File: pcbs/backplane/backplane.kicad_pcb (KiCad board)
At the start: 2 copper layers, 80 x 50 mm, 59 parts, among them P1 USB_B, P3 CONN_02X03, P4 CONN_02X03, P5 CONN_02X07, P6 CONN_02X07, P7 CONN_01X03, P8 CONN_01X03, Q1 MMBT3904, Q2 MMBT3904, Q3 Si2323, U1 LM358, U2 TC1262-33VDB, U3 LM358, U4 CH340G, Y1 Crystal

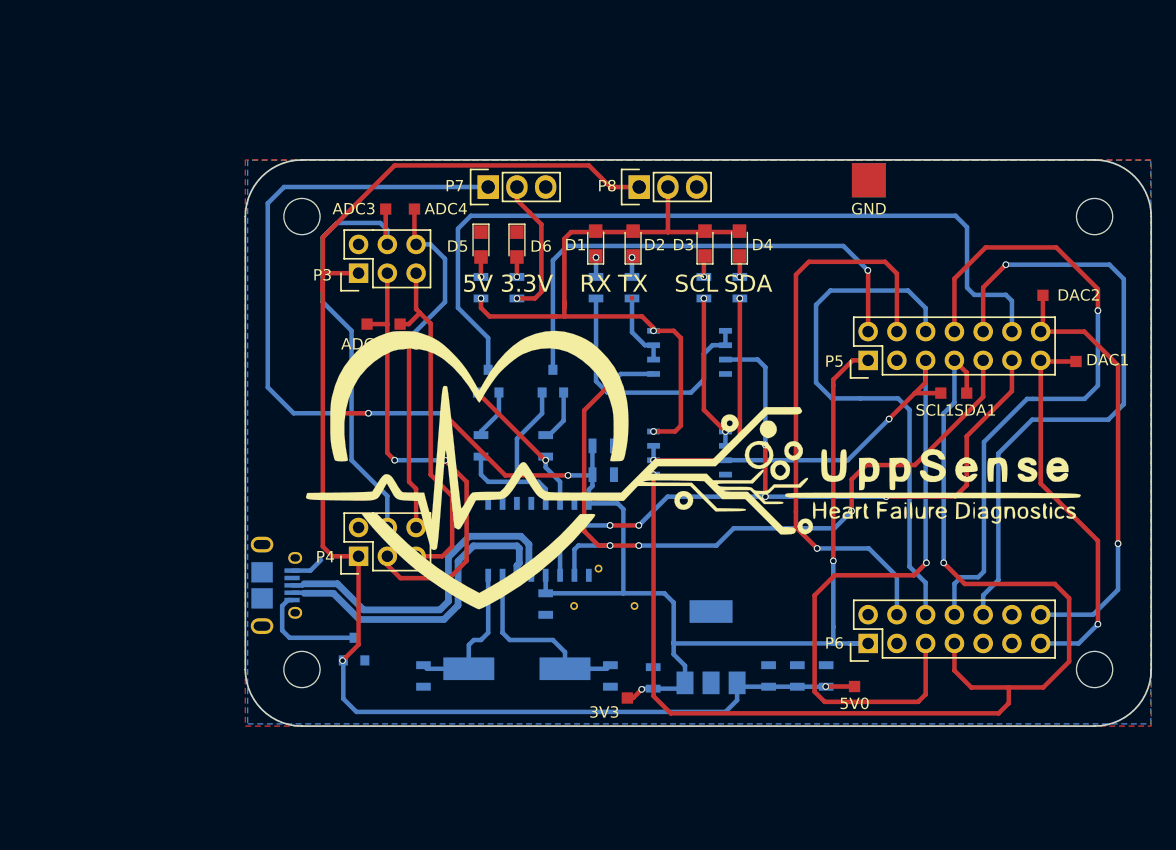
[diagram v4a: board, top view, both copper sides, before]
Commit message: Simulated the new transimpedance amp.
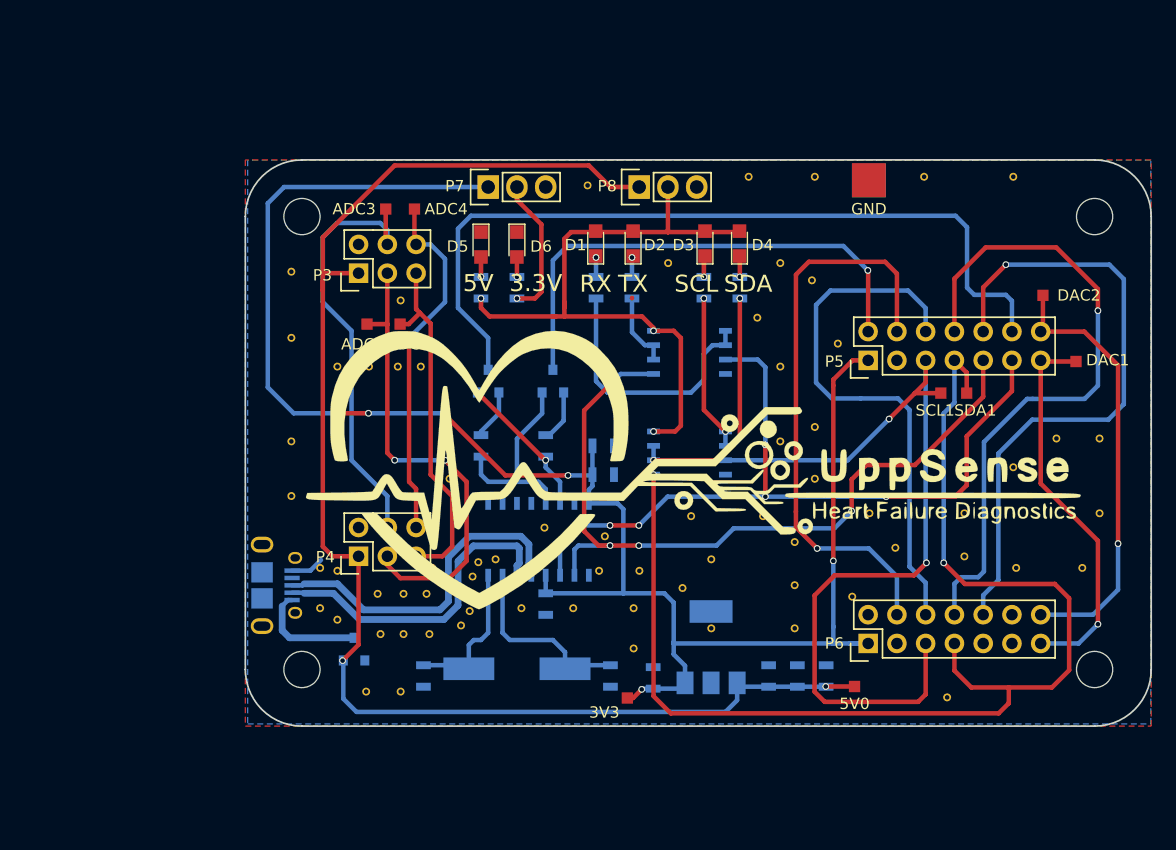
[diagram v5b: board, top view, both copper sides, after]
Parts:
- added REF**: Stitching-Via-0.5-0.7, myVias:Stitchging-Via-0.4-0.7, F.Cu at (182.3, 67.7)
- added REF**: Stitching-Via-0.5-0.7, myVias:Stitchging-Via-0.4-0.7, F.Cu at (122.6, 106.8)
- added REF**: Stitching-Via-0.5-0.7, myVias:Stitchging-Via-0.4-0.7, F.Cu at (121.1, 105.8)
- added REF**: Stitching-Via-0.5-0.7, myVias:Stitchging-Via-0.4-0.7, F.Cu at (122.6, 102.5)
- added REF**: Stitching-Via-0.5-0.7, myVias:Stitchging-Via-0.4-0.7, F.Cu at (134.3, 106.1)
- added REF**: Stitching-Via-0.5-0.7, myVias:Stitchging-Via-0.4-0.7, F.Cu at (134.5, 104.5)
- added REF**: Stitching-Via-0.5-0.7, myVias:Stitchging-Via-0.4-0.7, F.Cu at (130.7, 108.1)
- added REF**: Stitching-Via-0.5-0.7, myVias:Stitchging-Via-0.4-0.7, F.Cu at (126.4, 108.1)
- added REF**: Stitching-Via-0.5-0.7, myVias:Stitchging-Via-0.4-0.7, F.Cu at (130.5, 104.5)
- added REF**: Stitching-Via-0.5-0.7, myVias:Stitchging-Via-0.4-0.7, F.Cu at (126.2, 104.5)
- added REF**: Stitching-Via-0.5-0.7, myVias:Stitchging-Via-0.4-0.7, F.Cu at (164.8, 94.4)
- added REF**: Stitching-Via-0.5-0.7, myVias:Stitchging-Via-0.4-0.7, F.Cu at (174.4, 67.7)
- added REF**: Stitching-Via-0.5-0.7, myVias:Stitchging-Via-0.4-0.7, F.Cu at (164.8, 89.8)
- added REF**: Stitching-Via-0.5-0.7, myVias:Stitchging-Via-0.4-0.7, F.Cu at (166.8, 82.4)
- added REF**: Stitching-Via-0.5-0.7, myVias:Stitchging-Via-0.4-0.7, F.Cu at (164.5, 76.9)
- added REF**: Stitching-Via-0.5-0.7, myVias:Stitchging-Via-0.4-0.7, F.Cu at (144.7, 68.5)
- added REF**: Stitching-Via-0.5-0.7, myVias:Stitchging-Via-0.4-0.7, F.Cu at (128.2, 78.6)
- added REF**: Stitching-Via-0.5-0.7, myVias:Stitchging-Via-0.4-0.7, F.Cu at (132.5, 94.4)
- added REF**: Stitching-Via-0.5-0.7, myVias:Stitchging-Via-0.4-0.7, F.Cu at (130.0, 84.5)
- added REF**: Stitching-Via-0.5-0.7, myVias:Stitchging-Via-0.4-0.7, F.Cu at (127.9, 84.5)
- added REF**: Stitching-Via-0.5-0.7, myVias:Stitchging-Via-0.4-0.7, F.Cu at (125.4, 84.5)
- added REF**: Stitching-Via-0.5-0.7, myVias:Stitchging-Via-0.4-0.7, F.Cu at (122.6, 84.5)
- added REF**: Stitching-Via-0.5-0.7, myVias:Stitchging-Via-0.4-0.7, F.Cu at (164.8, 67.7)
- added REF**: Stitching-Via-0.5-0.7, myVias:Stitchging-Via-0.4-0.7, F.Cu at (118.5, 95.9)
- added REF**: Stitching-Via-0.5-0.7, myVias:Stitchging-Via-0.4-0.7, F.Cu at (118.5, 81.9)
- added REF**: Stitching-Via-0.5-0.7, myVias:Stitchging-Via-0.4-0.7, F.Cu at (118.5, 76.1)
- added REF**: Stitching-Via-0.5-0.7, myVias:Stitchging-Via-0.4-0.7, F.Cu at (118.5, 91.1)
- added REF**: Stitching-Via-0.5-0.7, myVias:Stitchging-Via-0.4-0.7, F.Cu at (121.1, 102.3)
- added REF**: Stitching-Via-0.5-0.7, myVias:Stitchging-Via-0.4-0.7, F.Cu at (128.4, 104.5)
- added REF**: Stitching-Via-0.5-0.7, myVias:Stitchging-Via-0.4-0.7, F.Cu at (133.5, 107.3)
- added REF**: Stitching-Via-0.5-0.7, myVias:Stitchging-Via-0.4-0.7, F.Cu at (134.5, 103.0)
- added REF**: Stitching-Via-0.5-0.7, myVias:Stitchging-Via-0.4-0.7, F.Cu at (128.2, 113.2)
- added REF**: Stitching-Via-0.5-0.7, myVias:Stitchging-Via-0.4-0.7, F.Cu at (128.4, 108.1)
- added REF**: Stitching-Via-0.5-0.7, myVias:Stitchging-Via-0.4-0.7, F.Cu at (158.9, 67.7)
- added REF**: Stitching-Via-0.5-0.7, myVias:Stitchging-Via-0.4-0.7, F.Cu at (125.1, 113.2)
- added REF**: Stitching-Via-0.5-0.7, myVias:Stitchging-Via-0.4-0.7, F.Cu at (140.9, 98.7)
- added REF**: Stitching-Via-0.5-0.7, myVias:Stitchging-Via-0.4-0.7, F.Cu at (146.2, 99.5)
- added REF**: Stitching-Via-0.5-0.7, myVias:Stitchging-Via-0.4-0.7, F.Cu at (160.2, 97.7)
- added REF**: Stitching-Via-0.5-0.7, myVias:Stitchging-Via-0.4-0.7, F.Cu at (153.8, 97.7)
- added REF**: Stitching-Via-0.5-0.7, myVias:Stitchging-Via-0.4-0.7, F.Cu at (151.8, 75.3)
- added REF**: Stitching-Via-0.5-0.7, myVias:Stitchging-Via-0.4-0.7, F.Cu at (159.7, 80.2)
- added REF**: Stitching-Via-0.5-0.7, myVias:Stitchging-Via-0.4-0.7, F.Cu at (161.7, 75.3)
- added REF**: Stitching-Via-0.5-0.7, myVias:Stitchging-Via-0.4-0.7, F.Cu at (161.7, 84.5)
- added REF**: Stitching-Via-0.5-0.7, myVias:Stitchging-Via-0.4-0.7, F.Cu at (161.7, 91.1)
- added REF**: Stitching-Via-0.5-0.7, myVias:Stitchging-Via-0.4-0.7, F.Cu at (168.1, 104.8)
- added REF**: Stitching-Via-0.5-0.7, myVias:Stitchging-Via-0.4-0.7, F.Cu at (189.9, 97.4)
- added REF**: Stitching-Via-0.5-0.7, myVias:Stitchging-Via-0.4-0.7, F.Cu at (186.1, 90.8)
- added REF**: Stitching-Via-0.5-0.7, myVias:Stitchging-Via-0.4-0.7, F.Cu at (189.9, 90.8)
- added REF**: Stitching-Via-0.5-0.7, myVias:Stitchging-Via-0.4-0.7, F.Cu at (188.4, 102.3)
- added REF**: Stitching-Via-0.5-0.7, myVias:Stitchging-Via-0.4-0.7, F.Cu at (182.3, 93.4)
- added REF**: Stitching-Via-0.5-0.7, myVias:Stitchging-Via-0.4-0.7, F.Cu at (182.5, 102.3)
- added REF**: Stitching-Via-0.5-0.7, myVias:Stitchging-Via-0.4-0.7, F.Cu at (178.0, 97.4)
- added REF**: Stitching-Via-0.5-0.7, myVias:Stitchging-Via-0.4-0.7, F.Cu at (178.0, 101.2)
- added REF**: Stitching-Via-0.5-0.7, myVias:Stitchging-Via-0.4-0.7, F.Cu at (169.6, 97.4)
- added REF**: Stitching-Via-0.5-0.7, myVias:Stitchging-Via-0.4-0.7, F.Cu at (171.9, 100.5)
- added REF**: Stitching-Via-0.5-0.7, myVias:Stitchging-Via-0.4-0.7, F.Cu at (176.5, 113.7)
- added REF**: Stitching-Via-0.5-0.7, myVias:Stitchging-Via-0.4-0.7, F.Cu at (155.6, 107.6)
- added REF**: Stitching-Via-0.5-0.7, myVias:Stitchging-Via-0.4-0.7, F.Cu at (153.1, 104.0)
- added REF**: Stitching-Via-0.5-0.7, myVias:Stitchging-Via-0.4-0.7, F.Cu at (149.3, 102.5)
- added REF**: Stitching-Via-0.5-0.7, myVias:Stitchging-Via-0.4-0.7, F.Cu at (155.6, 101.5)
- added REF**: Stitching-Via-0.5-0.7, myVias:Stitchging-Via-0.4-0.7, F.Cu at (163.0, 100.0)
- added REF**: Stitching-Via-0.5-0.7, myVias:Stitchging-Via-0.4-0.7, F.Cu at (163.0, 103.8)
- added REF**: Stitching-Via-0.5-0.7, myVias:Stitchging-Via-0.4-0.7, F.Cu at (163.0, 107.6)
- added REF**: Stitching-Via-0.5-0.7, myVias:Stitchging-Via-0.4-0.7, F.Cu at (138.9, 105.8)
- added REF**: Stitching-Via-0.5-0.7, myVias:Stitchging-Via-0.4-0.7, F.Cu at (148.8, 109.4)
- added REF**: Stitching-Via-0.5-0.7, myVias:Stitchging-Via-0.4-0.7, F.Cu at (131.0, 102.3)
- added REF**: Stitching-Via-0.5-0.7, myVias:Stitchging-Via-0.4-0.7, F.Cu at (136.6, 101.5)
- added REF**: Stitching-Via-0.5-0.7, myVias:Stitchging-Via-0.4-0.7, F.Cu at (135.1, 101.7)
- moved REF** 0.21 mm to (148.8, 105.8)
- moved REF** 0.21 mm to (143.4, 105.8)
- moved REF** 0.20 mm to (145.7, 102.5)
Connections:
- P1 pad : (no net) -> GND

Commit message: Added some iportant backplane spec.
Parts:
- removed the REF** at (134.5, 104.5)
- removed the REF** at (135.1, 101.7)
- moved REF** 0.80 mm to (134.5, 105.3)
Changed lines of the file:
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@@
 (kicad_pcb (version 4) (host pcbnew 4.0.6-e0-6349~52~ubuntu17.04.1)
   (general
-    (links 179)
+    (links 177)
     (no_connects 0)
     (area 114.400999 66.146999 194.551001 116.297001)
@@
     (tracks 460)
     (zones 0)
-    (modules 127)
+    (modules 125)
     (nets 41)
   )
@@
   )
   (setup
-    (last_trace_width 0.4)
+    (last_trace_width 0.25)
     (user_trace_width 0.2)
     (user_trace_width 0.3)
@@
   )
   (module myVias:Stitchging-Via-0.4-0.7 (layer F.Cu)
-    (at 135.05 101.744)
-    (fp_text reference REF** (at 0 1.27) (layer F.SilkS) hide
-      (effects (font (size 1 1) (thickness 0.15)))
-    )
-    (fp_text value Stitching-Via-0.5-0.7 (at 0 -1.27) (layer F.Fab)
-      (effects (font (size 1 1) (thickness 0.15)))
-    )
-    (pad "" thru_hole circle (at 0 0) (size 0.7 0.7) (drill 0.4) (layers *.Cu)
-      (net 1 GND) (zone_connect 2))
-  )
-  (module myVias:Stitchging-Via-0.4-0.7 (layer F.Cu)
     (at 122.604 106.824)
     (fp_text reference REF** (at 0 1.27) (layer F.SilkS) hide
@@
   )
   (module myVias:Stitchging-Via-0.4-0.7 (layer F.Cu)
-    (at 134.288 106.062)
-    (fp_text reference REF** (at 0 1.27) (layer F.SilkS) hide
-      (effects (font (size 1 1) (thickness 0.15)))
-    )
-    (fp_text value Stitching-Via-0.5-0.7 (at 0 -1.27) (layer F.Fab)
-      (effects (font (size 1 1) (thickness 0.15)))
-    )
-    (pad "" thru_hole circle (at 0 0) (size 0.7 0.7) (drill 0.4) (layers *.Cu)
-      (net 1 GND) (zone_connect 2))
-  )
-  (module myVias:Stitchging-Via-0.4-0.7 (layer F.Cu)
-    (at 134.542 104.538)
+    (at 134.542 105.3)
     (fp_text reference REF** (at 0 1.27) (layer F.SilkS) hide
       (effects (font (size 1 1) (thickness 0.15)))
@@
   (module myTestPoints:TP_SMD_quadr_1mm (layer F.Cu)
     (at 125.222 80.72)
-    (fp_text reference ADC1 (at -0.381 1.778) (layer F.SilkS)
+    (fp_text reference ADC1 (at -2.618 -0.058) (layer F.SilkS)
       (effects (font (size 1 1) (thickness 0.15)))
     )
@@
   (module myTestPoints:TP_SMD_quadr_1mm (layer F.Cu)
     (at 128.143 80.72)
-    (fp_text reference ADC2 (at 0.762 1.778) (layer F.SilkS)
+    (fp_text reference ADC2 (at 2.843 -0.058) (layer F.SilkS)
       (effects (font (size 1 1) (thickness 0.15)))
     )
@@
   (module myTestPoints:TP_SMD_quadr_1mm (layer F.Cu)
     (at 175.895 86.816)
-    (fp_text reference SCL1 (at -0.508 1.524) (layer F.SilkS)
+    (fp_text reference SCL1 (at -0.713 1.466) (layer F.SilkS)
       (effects (font (size 1 1) (thickness 0.15)))
     )
@@
   (module myTestPoints:TP_SMD_quadr_1mm (layer F.Cu)
     (at 178.181 86.816)
-    (fp_text reference SDA1 (at 0.762 1.524) (layer F.SilkS)
-      (effects (font (size 1 1) (thickness 0.15)))
-    )
+    (fp_text reference SDA1 (at 1.065 1.466) (layer F.SilkS)
+      (effects (font (size 1 1) (thickness 0.15)))
+    )

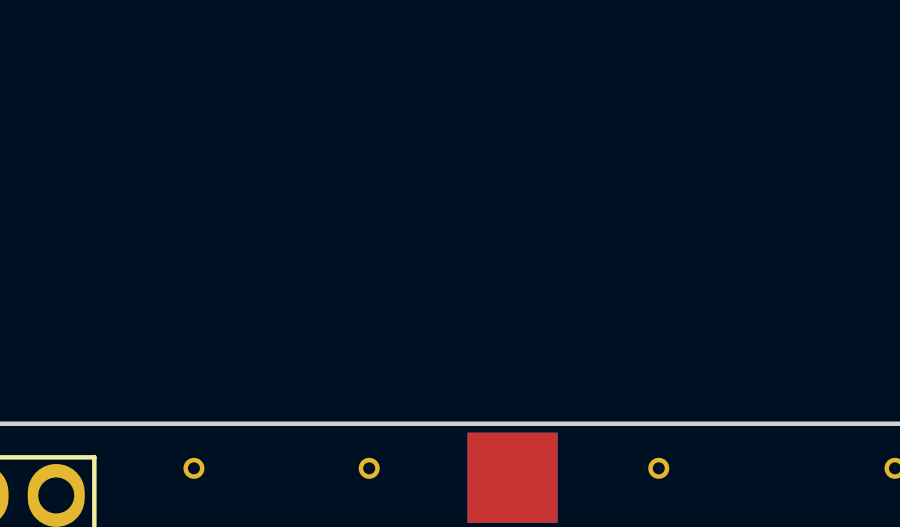
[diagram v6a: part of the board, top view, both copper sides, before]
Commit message: Small changes on the backplane standing out.
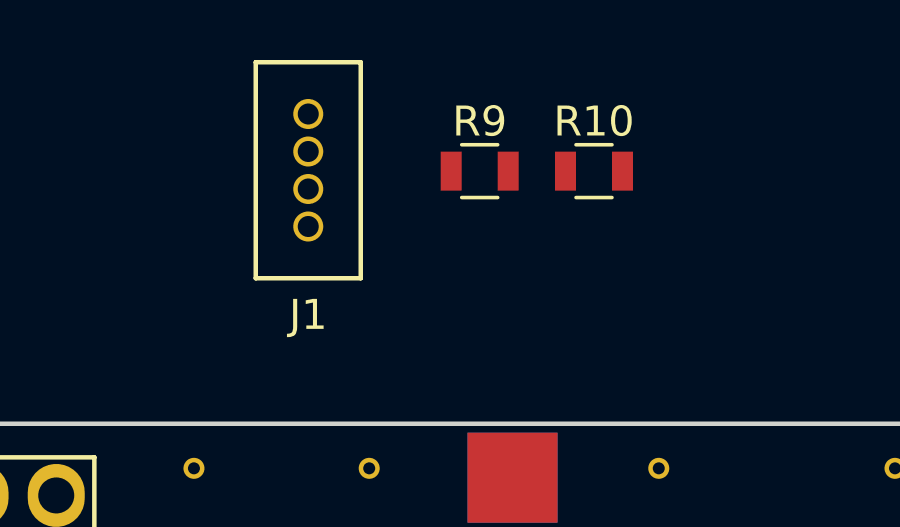
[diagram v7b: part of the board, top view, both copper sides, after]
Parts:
- added J1: CONN_01X04, ConnectorsChina:LED_CONN_1.25_PITCH, F.Cu at (162.7, 55.9)
- added R10: 470R, Resistors_SMD:R_0805, F.Cu at (172.3, 57.8)
- added R9: 470R, Resistors_SMD:R_0805, F.Cu at (168.5, 57.8)
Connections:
- P1 pad : GND -> (no net)
- P1 pad 1: Net-(P1-Pad1) -> 5V_USB
- P8 pad 1: 5V -> 5V_USB
- P8 pad 2: LED_5V -> Net-(P8-Pad2)
- P8 pad 3: (no net) -> 5V_BATT
- Q3 pad 3: Net-(P1-Pad1) -> Net-(P8-Pad2)
- U4 pad 2: UART_TX -> Net-(R9-Pad1)
- U4 pad 3: UART_RX -> Net-(R10-Pad1)
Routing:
- net Net-(P1-Pad1): track 9.87 -> 0.00 mm
- net Net-(P8-Pad2): track 0.00 -> 9.68 mm
- net 5V_USB: track 0.00 -> 6.71 mm
- net LED_5V: track 57.8 -> 53.8 mm
- net UART_RX: track 68.9 -> 65.9 mm
- net Net-(R10-Pad1): track 0.00 -> 3.04 mm
- net 5V: track 127.3 -> 124.7 mm
- net UART_TX: track 69.8 -> 67.5 mm
- net Net-(R9-Pad1): track 0.00 -> 2.27 mm

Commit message: Backplane definitely finished. Somethings wrong with TIA. Has to be checked tomorrow.
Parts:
- removed the REF** at (182.3, 67.7)
- removed the REF** at (121.1, 105.8)
- removed the REF** at (122.6, 102.5)
- removed the REF** at (134.5, 105.3)
- removed the REF** at (130.7, 108.1)
- removed the REF** at (126.4, 108.1)
- removed the REF** at (130.5, 104.5)
- removed the REF** at (126.2, 104.5)
- removed the REF** at (164.8, 94.4)
- removed the REF** at (164.8, 89.8)
- removed the REF** at (166.8, 82.4)
- removed the REF** at (174.4, 67.7)
- removed the REF** at (164.5, 76.9)
- removed the REF** at (144.7, 68.5)
- removed the REF** at (128.2, 78.6)
- removed the REF** at (132.5, 94.4)
- removed the REF** at (130.0, 84.5)
- removed the REF** at (127.9, 84.5)
- removed the REF** at (125.4, 84.5)
- removed the REF** at (122.6, 84.5)
- removed the REF** at (118.5, 95.9)
- removed the REF** at (118.5, 81.9)
- removed the REF** at (164.8, 67.7)
- removed the REF** at (118.5, 76.1)
- removed the REF** at (118.5, 91.1)
- removed the REF** at (121.1, 102.3)
- removed the REF** at (128.4, 104.5)
- removed the REF** at (133.5, 107.3)
- removed the REF** at (134.5, 103.0)
- removed the REF** at (128.2, 113.2)
- removed the REF** at (128.4, 108.1)
- removed the REF** at (125.1, 113.2)
- removed the REF** at (140.9, 98.7)
- removed the REF** at (158.9, 67.7)
- removed the REF** at (146.2, 99.5)
- removed the REF** at (160.2, 97.7)
- removed the REF** at (153.8, 97.7)
- removed the REF** at (151.8, 75.3)
- removed the REF** at (159.7, 80.2)
- removed the REF** at (161.7, 75.3)
- removed the REF** at (161.7, 84.5)
- removed the REF** at (161.7, 91.1)
- removed the REF** at (189.9, 97.4)
- removed the REF** at (186.1, 90.8)
- removed the REF** at (168.1, 104.8)
- removed the REF** at (189.9, 90.8)
- removed the REF** at (188.4, 102.3)
- removed the REF** at (182.3, 93.4)
- removed the REF** at (182.5, 102.3)
- removed the REF** at (178.0, 97.4)
- removed the REF** at (178.0, 101.2)
- removed the REF** at (169.6, 97.4)
- removed the REF** at (171.9, 100.5)
- removed the REF** at (155.6, 107.6)
- removed the REF** at (153.1, 104.0)
- removed the REF** at (176.5, 113.7)
- removed the REF** at (149.3, 102.5)
- removed the REF** at (155.6, 101.5)
- removed the REF** at (163.0, 100.0)
- removed the REF** at (163.0, 103.8)
- removed the REF** at (163.0, 107.6)
- removed the REF** at (138.9, 105.8)
- removed the REF** at (148.8, 109.4)
- removed the REF** at (148.8, 105.8)
- removed the REF** at (143.4, 105.8)
- removed the REF** at (145.7, 102.5)
- removed the REF** at (131.0, 102.3)
- removed the REF** at (136.6, 101.5)
- removed the REF** at (122.6, 106.8)
- added C10: 10u, Resistors_SMD:R_0805, B.Cu at (150.8, 77.5)
- added C11: 10u, Resistors_SMD:R_0805, B.Cu at (149.5, 88.8)
- added C12: 100n, Resistors_SMD:R_0805, B.Cu at (152.8, 77.5)
- added C13: 100n, Resistors_SMD:R_0805, B.Cu at (149.5, 86.8)
- added P2: CONN_01X03, mySamtec:Samtec-PHT-1-3-01-L-S, F.Cu at (146.2, 68.6)
- added REF**: Stitching-Via-0.4-0.7, myVias:Stitchging-Via-0.4-0.7, F.Cu at (134.2, 107.2)
- added REF**: Stitching-Via-0.4-0.7, myVias:Stitchging-Via-0.4-0.7, F.Cu at (154.2, 114.1)
- added REF**: Stitching-Via-0.4-0.7, myVias:Stitchging-Via-0.4-0.7, F.Cu at (160.9, 104.9)
- added REF**: Stitching-Via-0.4-0.7, myVias:Stitchging-Via-0.4-0.7, F.Cu at (160.9, 102.3)
- added REF**: Stitching-Via-0.4-0.7, myVias:Stitchging-Via-0.4-0.7, F.Cu at (160.9, 82.0)
- added REF**: Stitching-Via-0.4-0.7, myVias:Stitchging-Via-0.4-0.7, F.Cu at (160.9, 76.9)
- added REF**: Stitching-Via-0.4-0.7, myVias:Stitchging-Via-0.4-0.7, F.Cu at (160.9, 79.5)
- added REF**: Stitching-Via-0.4-0.7, myVias:Stitchging-Via-0.4-0.7, F.Cu at (160.9, 107.4)
- added REF**: Stitching-Via-0.4-0.7, myVias:Stitchging-Via-0.4-0.7, F.Cu at (160.9, 87.1)
- added REF**: Stitching-Via-0.4-0.7, myVias:Stitchging-Via-0.4-0.7, F.Cu at (160.9, 94.7)
- added REF**: Stitching-Via-0.4-0.7, myVias:Stitchging-Via-0.4-0.7, F.Cu at (173.9, 68.5)
- added REF**: Stitching-Via-0.4-0.7, myVias:Stitchging-Via-0.4-0.7, F.Cu at (156.1, 68.5)
- added REF**: Stitching-Via-0.4-0.7, myVias:Stitchging-Via-0.4-0.7, F.Cu at (179.6, 114.1)
- added REF**: Stitching-Via-0.4-0.7, myVias:Stitchging-Via-0.4-0.7, F.Cu at (176.5, 68.5)
- added REF**: Stitching-Via-0.4-0.7, myVias:Stitchging-Via-0.4-0.7, F.Cu at (181.5, 68.5)
- added REF**: Stitching-Via-0.4-0.7, myVias:Stitchging-Via-0.4-0.7, F.Cu at (161.2, 68.5)
- added REF**: Stitching-Via-0.4-0.7, myVias:Stitchging-Via-0.4-0.7, F.Cu at (158.7, 68.5)
- added REF**: Stitching-Via-0.4-0.7, myVias:Stitchging-Via-0.4-0.7, F.Cu at (179.0, 68.5)
- added REF**: Stitching-Via-0.4-0.7, myVias:Stitchging-Via-0.4-0.7, F.Cu at (168.8, 68.5)
- added REF**: Stitching-Via-0.4-0.7, myVias:Stitchging-Via-0.4-0.7, F.Cu at (171.4, 68.5)
- added REF**: Stitching-Via-0.4-0.7, myVias:Stitchging-Via-0.4-0.7, F.Cu at (186.6, 68.5)
- added REF**: Stitching-Via-0.4-0.7, myVias:Stitchging-Via-0.4-0.7, F.Cu at (166.3, 68.5)
- added REF**: Stitching-Via-0.4-0.7, myVias:Stitchging-Via-0.4-0.7, F.Cu at (163.8, 68.5)
- added REF**: Stitching-Via-0.4-0.7, myVias:Stitchging-Via-0.4-0.7, F.Cu at (159.3, 114.1)
- added REF**: Stitching-Via-0.4-0.7, myVias:Stitchging-Via-0.4-0.7, F.Cu at (184.1, 68.5)
- added REF**: Stitching-Via-0.4-0.7, myVias:Stitchging-Via-0.4-0.7, F.Cu at (143.4, 68.5)
- added REF**: Stitching-Via-0.4-0.7, myVias:Stitchging-Via-0.4-0.7, F.Cu at (153.8, 109.9)
- added REF**: Stitching-Via-0.4-0.7, myVias:Stitchging-Via-0.4-0.7, F.Cu at (156.4, 109.9)
- added REF**: Stitching-Via-0.4-0.7, myVias:Stitchging-Via-0.4-0.7, F.Cu at (161.5, 109.9)
- added REF**: Stitching-Via-0.4-0.7, myVias:Stitchging-Via-0.4-0.7, F.Cu at (158.9, 109.9)
- added REF**: Stitching-Via-0.4-0.7, myVias:Stitchging-Via-0.4-0.7, F.Cu at (191.9, 109.9)
- added REF**: Stitching-Via-0.4-0.7, myVias:Stitchging-Via-0.4-0.7, F.Cu at (166.5, 109.9)
- added REF**: Stitching-Via-0.4-0.7, myVias:Stitchging-Via-0.4-0.7, F.Cu at (138.6, 109.9)
- added REF**: Stitching-Via-0.4-0.7, myVias:Stitchging-Via-0.4-0.7, F.Cu at (156.8, 114.1)
- added REF**: Stitching-Via-0.4-0.7, myVias:Stitchging-Via-0.4-0.7, F.Cu at (177.1, 114.1)
- added REF**: Stitching-Via-0.4-0.7, myVias:Stitchging-Via-0.4-0.7, F.Cu at (184.7, 114.1)
- added REF**: Stitching-Via-0.4-0.7, myVias:Stitchging-Via-0.4-0.7, F.Cu at (164.4, 114.1)
- added REF**: Stitching-Via-0.4-0.7, myVias:Stitchging-Via-0.4-0.7, F.Cu at (161.8, 114.1)
- added REF**: Stitching-Via-0.4-0.7, myVias:Stitchging-Via-0.4-0.7, F.Cu at (141.5, 114.1)
- added REF**: Stitching-Via-0.4-0.7, myVias:Stitchging-Via-0.4-0.7, F.Cu at (121.2, 114.1)
- added REF**: Stitching-Via-0.4-0.7, myVias:Stitchging-Via-0.4-0.7, F.Cu at (121.3, 105.9)
- added REF**: Stitching-Via-0.4-0.7, myVias:Stitchging-Via-0.4-0.7, F.Cu at (123.7, 114.1)
- added REF**: Stitching-Via-0.4-0.7, myVias:Stitchging-Via-0.4-0.7, F.Cu at (144.1, 114.1)
- added REF**: Stitching-Via-0.4-0.7, myVias:Stitchging-Via-0.4-0.7, F.Cu at (146.6, 114.1)
- added REF**: Stitching-Via-0.4-0.7, myVias:Stitchging-Via-0.4-0.7, F.Cu at (136.4, 114.1)
- added REF**: Stitching-Via-0.4-0.7, myVias:Stitchging-Via-0.4-0.7, F.Cu at (118.7, 114.1)
- added REF**: Stitching-Via-0.4-0.7, myVias:Stitchging-Via-0.4-0.7, F.Cu at (139.0, 114.1)
- added REF**: Stitching-Via-0.4-0.7, myVias:Stitchging-Via-0.4-0.7, F.Cu at (133.9, 114.1)
- added REF**: Stitching-Via-0.4-0.7, myVias:Stitchging-Via-0.4-0.7, F.Cu at (167.4, 76.5)
- added REF**: Stitching-Via-0.4-0.7, myVias:Stitchging-Via-0.4-0.7, F.Cu at (167.5, 72.1)
- added REF**: Stitching-Via-0.4-0.7, myVias:Stitchging-Via-0.4-0.7, F.Cu at (167.5, 107.6)
- added REF**: Stitching-Via-0.4-0.7, myVias:Stitchging-Via-0.4-0.7, F.Cu at (134.7, 104.7)
- added REF**: Stitching-Via-0.4-0.7, myVias:Stitchging-Via-0.4-0.7, F.Cu at (167.5, 105.1)
- added REF**: Stitching-Via-0.4-0.7, myVias:Stitchging-Via-0.4-0.7, F.Cu at (167.5, 84.8)
- added REF**: Stitching-Via-0.4-0.7, myVias:Stitchging-Via-0.4-0.7, F.Cu at (167.5, 79.7)
- added REF**: Stitching-Via-0.4-0.7, myVias:Stitchging-Via-0.4-0.7, F.Cu at (167.5, 82.2)
- added REF**: Stitching-Via-0.4-0.7, myVias:Stitchging-Via-0.4-0.7, F.Cu at (148.5, 108.2)
- added REF**: Stitching-Via-0.4-0.7, myVias:Stitchging-Via-0.4-0.7, F.Cu at (148.5, 105.7)
- added REF**: Stitching-Via-0.4-0.7, myVias:Stitchging-Via-0.4-0.7, F.Cu at (148.5, 85.4)
- added REF**: Stitching-Via-0.4-0.7, myVias:Stitchging-Via-0.4-0.7, F.Cu at (149.0, 100.6)
- added REF**: Stitching-Via-0.4-0.7, myVias:Stitchging-Via-0.4-0.7, F.Cu at (148.5, 82.8)
- added REF**: Stitching-Via-0.4-0.7, myVias:Stitchging-Via-0.4-0.7, F.Cu at (148.5, 93.0)
- added REF**: Stitching-Via-0.4-0.7, myVias:Stitchging-Via-0.4-0.7, F.Cu at (134.7, 102.1)
- added REF**: Stitching-Via-0.4-0.7, myVias:Stitchging-Via-0.4-0.7, F.Cu at (148.5, 110.8)
- added REF**: Stitching-Via-0.4-0.7, myVias:Stitchging-Via-0.4-0.7, F.Cu at (148.5, 90.4)
- added REF**: Stitching-Via-0.4-0.7, myVias:Stitchging-Via-0.4-0.7, F.Cu at (148.5, 95.5)
- added REF**: Stitching-Via-0.4-0.7, myVias:Stitchging-Via-0.4-0.7, F.Cu at (187.2, 71.9)
- added REF**: Stitching-Via-0.4-0.7, myVias:Stitchging-Via-0.4-0.7, F.Cu at (187.2, 102.4)
- added REF**: Stitching-Via-0.4-0.7, myVias:Stitchging-Via-0.4-0.7, F.Cu at (187.2, 77.0)
- added REF**: Stitching-Via-0.4-0.7, myVias:Stitchging-Via-0.4-0.7, F.Cu at (187.2, 99.8)
- added REF**: Stitching-Via-0.4-0.7, myVias:Stitchging-Via-0.4-0.7, F.Cu at (187.2, 79.5)
- added REF**: Stitching-Via-0.4-0.7, myVias:Stitchging-Via-0.4-0.7, F.Cu at (187.2, 89.7)
- added REF**: Stitching-Via-0.4-0.7, myVias:Stitchging-Via-0.4-0.7, F.Cu at (187.2, 87.1)
- added REF**: Stitching-Via-0.4-0.7, myVias:Stitchging-Via-0.4-0.7, F.Cu at (122.8, 102.4)
- added REF**: Stitching-Via-0.4-0.7, myVias:Stitchging-Via-0.4-0.7, F.Cu at (187.2, 92.2)
- added REF**: Stitching-Via-0.4-0.7, myVias:Stitchging-Via-0.4-0.7, F.Cu at (187.2, 112.5)
- added REF**: Stitching-Via-0.4-0.7, myVias:Stitchging-Via-0.4-0.7, F.Cu at (187.2, 115.1)
- added REF**: Stitching-Via-0.4-0.7, myVias:Stitchging-Via-0.4-0.7, F.Cu at (187.2, 95.5)
- added REF**: Stitching-Via-0.4-0.7, myVias:Stitchging-Via-0.4-0.7, F.Cu at (177.3, 98.6)
- added REF**: Stitching-Via-0.4-0.7, myVias:Stitchging-Via-0.4-0.7, F.Cu at (179.9, 98.6)
- added REF**: Stitching-Via-0.4-0.7, myVias:Stitchging-Via-0.4-0.7, F.Cu at (184.3, 98.6)
- added REF**: Stitching-Via-0.4-0.7, myVias:Stitchging-Via-0.4-0.7, F.Cu at (164.6, 98.6)
- added REF**: Stitching-Via-0.4-0.7, myVias:Stitchging-Via-0.4-0.7, F.Cu at (161.1, 98.6)
- added REF**: Stitching-Via-0.4-0.7, myVias:Stitchging-Via-0.4-0.7, F.Cu at (192.6, 98.6)
- added REF**: Stitching-Via-0.4-0.7, myVias:Stitchging-Via-0.4-0.7, F.Cu at (120.3, 102.4)
- added REF**: Stitching-Via-0.4-0.7, myVias:Stitchging-Via-0.4-0.7, F.Cu at (172.3, 98.6)
- added REF**: Stitching-Via-0.4-0.7, myVias:Stitchging-Via-0.4-0.7, F.Cu at (190.0, 98.6)
- added REF**: Stitching-Via-0.4-0.7, myVias:Stitchging-Via-0.4-0.7, F.Cu at (169.7, 98.6)
- added REF**: Stitching-Via-0.4-0.7, myVias:Stitchging-Via-0.4-0.7, F.Cu at (167.4, 98.6)
- added REF**: Stitching-Via-0.4-0.7, myVias:Stitchging-Via-0.4-0.7, F.Cu at (132.5, 94.5)
- added REF**: Stitching-Via-0.4-0.7, myVias:Stitchging-Via-0.4-0.7, F.Cu at (131.6, 98.6)
- added REF**: Stitching-Via-0.4-0.7, myVias:Stitchging-Via-0.4-0.7, F.Cu at (141.8, 98.6)
- added REF**: Stitching-Via-0.4-0.7, myVias:Stitchging-Via-0.4-0.7, F.Cu at (144.3, 98.6)
- added REF**: Stitching-Via-0.4-0.7, myVias:Stitchging-Via-0.4-0.7, F.Cu at (139.2, 98.6)
- added REF**: Stitching-Via-0.4-0.7, myVias:Stitchging-Via-0.4-0.7, F.Cu at (136.7, 98.6)
- added REF**: Stitching-Via-0.4-0.7, myVias:Stitchging-Via-0.4-0.7, F.Cu at (125.6, 104.6)
- added REF**: Stitching-Via-0.4-0.7, myVias:Stitchging-Via-0.4-0.7, F.Cu at (127.9, 83.3)
- added REF**: Stitching-Via-0.4-0.7, myVias:Stitchging-Via-0.4-0.7, F.Cu at (129.8, 83.3)
- added REF**: Stitching-Via-0.4-0.7, myVias:Stitchging-Via-0.4-0.7, F.Cu at (134.8, 83.3)
- added REF**: Stitching-Via-0.4-0.7, myVias:Stitchging-Via-0.4-0.7, F.Cu at (132.9, 83.3)
- added REF**: Stitching-Via-0.4-0.7, myVias:Stitchging-Via-0.4-0.7, F.Cu at (143.1, 83.3)
- added REF**: Stitching-Via-0.4-0.7, myVias:Stitchging-Via-0.4-0.7, F.Cu at (140.5, 83.3)
- added REF**: Stitching-Via-0.4-0.7, myVias:Stitchging-Via-0.4-0.7, F.Cu at (138.0, 83.3)
- added REF**: Stitching-Via-0.4-0.7, myVias:Stitchging-Via-0.4-0.7, F.Cu at (125.3, 83.3)
- added REF**: Stitching-Via-0.4-0.7, myVias:Stitchging-Via-0.4-0.7, F.Cu at (122.7, 83.3)
- added REF**: Stitching-Via-0.4-0.7, myVias:Stitchging-Via-0.4-0.7, F.Cu at (170.6, 96.3)
- added REF**: Stitching-Via-0.4-0.7, myVias:Stitchging-Via-0.4-0.7, F.Cu at (130.7, 104.6)
- added REF**: Stitching-Via-0.4-0.7, myVias:Stitchging-Via-0.4-0.7, F.Cu at (152.8, 96.3)
- added REF**: Stitching-Via-0.4-0.7, myVias:Stitchging-Via-0.4-0.7, F.Cu at (178.2, 96.3)
- added REF**: Stitching-Via-0.4-0.7, myVias:Stitchging-Via-0.4-0.7, F.Cu at (157.9, 96.3)
- added REF**: Stitching-Via-0.4-0.7, myVias:Stitchging-Via-0.4-0.7, F.Cu at (155.4, 96.3)
- added REF**: Stitching-Via-0.4-0.7, myVias:Stitchging-Via-0.4-0.7, F.Cu at (168.1, 96.3)
- added REF**: Stitching-Via-0.4-0.7, myVias:Stitchging-Via-0.4-0.7, F.Cu at (183.3, 96.3)
- added REF**: Stitching-Via-0.4-0.7, myVias:Stitchging-Via-0.4-0.7, F.Cu at (122.3, 96.3)
- added REF**: Stitching-Via-0.4-0.7, myVias:Stitchging-Via-0.4-0.7, F.Cu at (124.9, 96.3)
- added REF**: Stitching-Via-0.4-0.7, myVias:Stitchging-Via-0.4-0.7, F.Cu at (119.9, 67.4)
- added REF**: Stitching-Via-0.4-0.7, myVias:Stitchging-Via-0.4-0.7, F.Cu at (119.9, 85.2)
- added REF**: Stitching-Via-0.4-0.7, myVias:Stitchging-Via-0.4-0.7, F.Cu at (128.1, 104.6)
- added REF**: Stitching-Via-0.4-0.7, myVias:Stitchging-Via-0.4-0.7, F.Cu at (119.9, 80.1)
- added REF**: Stitching-Via-0.4-0.7, myVias:Stitchging-Via-0.4-0.7, F.Cu at (119.9, 82.6)
- added REF**: Stitching-Via-0.4-0.7, myVias:Stitchging-Via-0.4-0.7, F.Cu at (119.9, 75.0)
- added REF**: Stitching-Via-0.4-0.7, myVias:Stitchging-Via-0.4-0.7, F.Cu at (119.9, 77.6)
- added REF**: Stitching-Via-0.4-0.7, myVias:Stitchging-Via-0.4-0.7, F.Cu at (119.9, 97.9)
- added REF**: Stitching-Via-0.4-0.7, myVias:Stitchging-Via-0.4-0.7, F.Cu at (119.9, 95.3)
- added REF**: Stitching-Via-0.4-0.7, myVias:Stitchging-Via-0.4-0.7, F.Cu at (119.9, 90.3)
- added REF**: Stitching-Via-0.4-0.7, myVias:Stitchging-Via-0.4-0.7, F.Cu at (119.9, 92.8)
- added REF**: Stitching-Via-0.4-0.7, myVias:Stitchging-Via-0.4-0.7, F.Cu at (119.9, 100.4)
- added REF**: Stitching-Via-0.4-0.7, myVias:Stitchging-Via-0.4-0.7, F.Cu at (160.9, 84.5)
- J1, R10, R9: moved to B.Cu
- moved J1 55.7 mm to (146.9, 109.2)
- moved P8 47.5 mm to (124.6, 109.2)
- moved R9 33.5 mm to (179.6, 89.4), turned to 90 degrees
- moved R10 33.1 mm to (182.2, 89.4), turned to 90 degrees
- moved G*** 5.79 mm to (159.4, 92.1)
- moved Q3 4.77 mm to (127.2, 113.0)
- moved C7 1.38 mm to (130.2, 113.2)
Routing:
- net Net-(R10-Pad1): track 3.04 -> 49.6 mm, vias 0 -> 4
- net Net-(R9-Pad1): track 2.27 -> 43.9 mm, vias 0 -> 4
- net UART_RX: track 65.9 -> 43.4 mm, vias 5 -> 2
- net UART_TX: track 67.5 -> 48.4 mm, vias 4 -> 1
- net 5V_BATT: track 0.00 -> 18.9 mm
- net 5V: track 124.7 -> 139.6 mm
- net LED_5V: track 53.8 -> 65.8 mm
- net Net-(P8-Pad2): track 9.68 -> 2.81 mm
- net 5V_USB: track 6.71 -> 11.1 mm
- net GPIO3: track 58.6 -> 55.0 mm
- net 3.3V: track 157.5 -> 160.3 mm
- net GPIO4: track 56.4 -> 54.2 mm
- net Net-(C7-Pad1): track 13.5 -> 14.7 mm
- net Net-(R1-Pad2): track 23.5 -> 23.4 mm, vias 0 -> 2
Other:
- board text added: "BAT"
- board text added: "BAT CONN"
- board text added: "GND"
- board text added: "POWER"
- board text added: "USB"
